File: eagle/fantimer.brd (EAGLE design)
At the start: 58 x 78 mm, 14 parts, among them IC3 PIC10F220, K1 PB2032-ND, Q1 2N7000-G, U1 IRM-01-5, X1 732-10957-ND

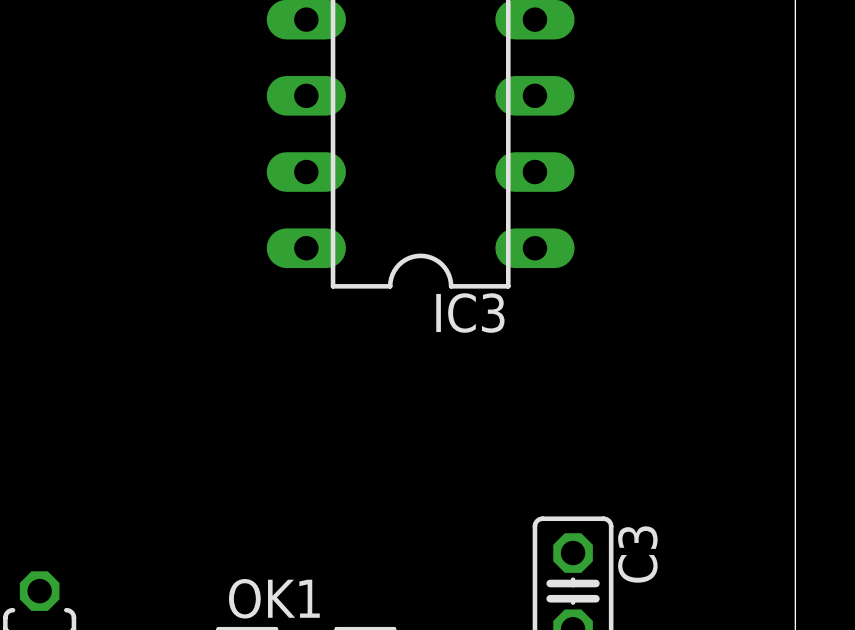
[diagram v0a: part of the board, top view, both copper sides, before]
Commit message: Renumber IC3 to IC1
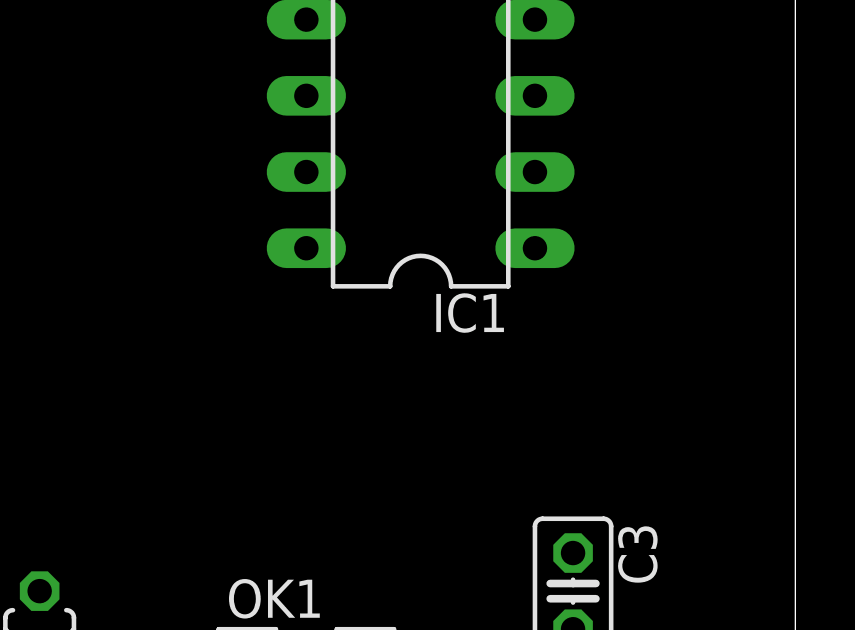
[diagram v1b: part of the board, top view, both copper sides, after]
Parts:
- renumbered IC3 to IC1
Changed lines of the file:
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@@
 <attribute name="SPICEPREFIX" value="X" x="45.72" y="48.26" size="1.778" layer="27" rot="R270" display="off"/>
 </element>
-<element name="IC3" library="ic-package" library_urn="urn:adsk.eagle:library:239" package="DIL08" package3d_urn="urn:adsk.eagle:package:14440/1" value="PIC10F220" x="43.18" y="22.86" rot="R90"/>
+<element name="IC1" library="ic-package" library_urn="urn:adsk.eagle:library:239" package="DIL08" package3d_urn="urn:adsk.eagle:package:14440/1" value="PIC10F220" x="43.18" y="22.86" rot="R90"/>
 <element name="C3" library="rcl" library_urn="urn:adsk.eagle:library:334" package="C025-025X050" package3d_urn="urn:adsk.eagle:package:23629/2" value="1uF" x="48.26" y="7.62" rot="R270">
 <attribute name="SPICEPREFIX" value="C" x="48.26" y="7.62" size="1.778" layer="27" rot="R270" display="off"/>
@@
 <signal name="FAN">
 <contactref element="Q1" pad="2"/>
-<contactref element="IC3" pad="5"/>
+<contactref element="IC1" pad="5"/>
 <wire x1="39.37" y1="26.67" x2="36.195" y2="35.56" width="0" layer="19" extent="1-1"/>
 </signal>
@@
 <signal name="!LIGHT">
 <contactref element="OK1" pad="4"/>
-<contactref element="IC3" pad="8"/>
+<contactref element="IC1" pad="8"/>
 <contactref element="C3" pad="2"/>
 <wire x1="43.18" y1="5.08" x2="39.37" y2="19.05" width="0" layer="19" extent="1-1"/>
@@
 <signal name="RTIMER">
 <contactref element="R3" pad="3"/>
-<contactref element="IC3" pad="4"/>
+<contactref element="IC1" pad="4"/>
 <wire x1="46.99" y1="26.67" x2="50.8" y2="48.26" width="0" layer="19" extent="1-1"/>
 </signal>
@@
 <contactref element="U1" pad="-V"/>
 <contactref element="OK1" pad="3"/>
-<contactref element="IC3" pad="7"/>
+<contactref element="IC1" pad="7"/>
 <contactref element="R3" pad="2"/>
 <wire x1="30.48" y1="45.74" x2="40.64" y2="45.72" width="0" layer="19" extent="1-1"/>
@@
 <contactref element="D1" pad="C"/>
 <contactref element="U1" pad="+V"/>
-<contactref element="IC3" pad="2"/>
+<contactref element="IC1" pad="2"/>
 <contactref element="R3" pad="1"/>
 <contactref element="C3" pad="1"/>

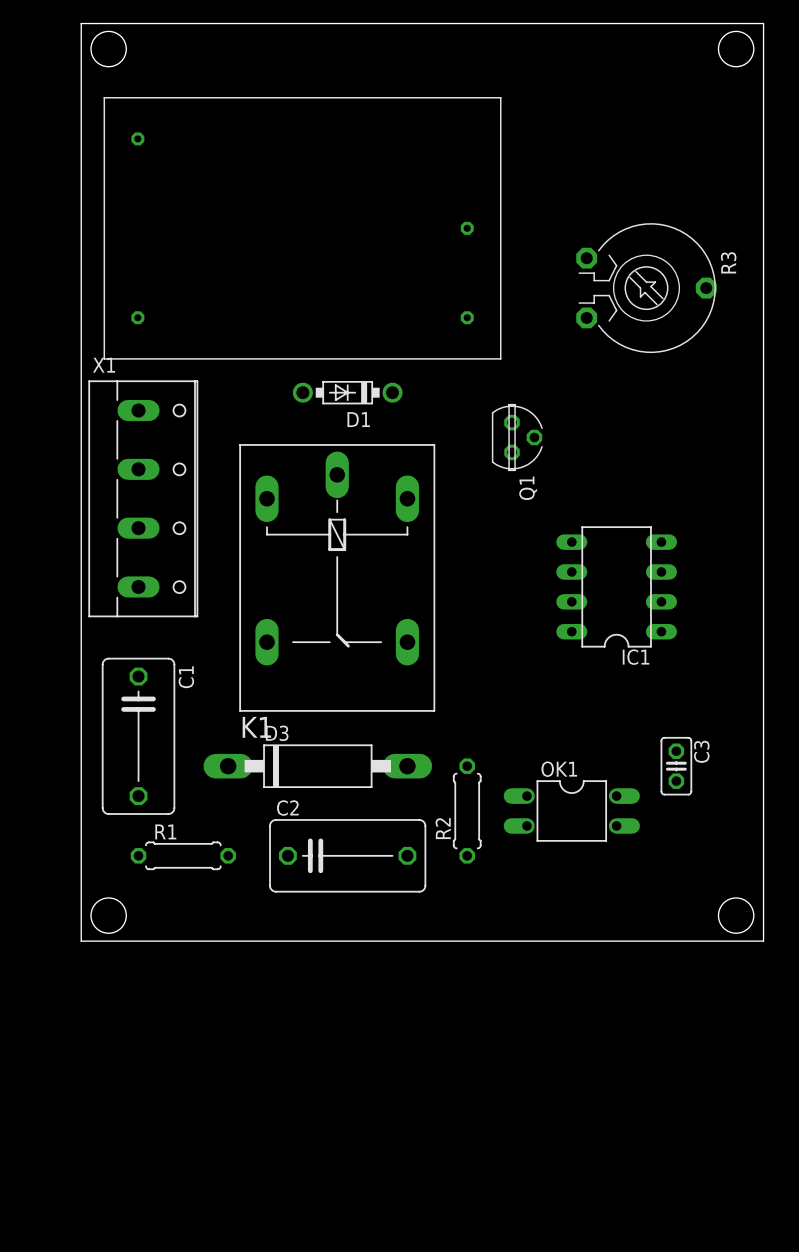
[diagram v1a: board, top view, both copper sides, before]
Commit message: Initial assembly. Add a better PIC Eagle lib. Remove PIC notes from sch.
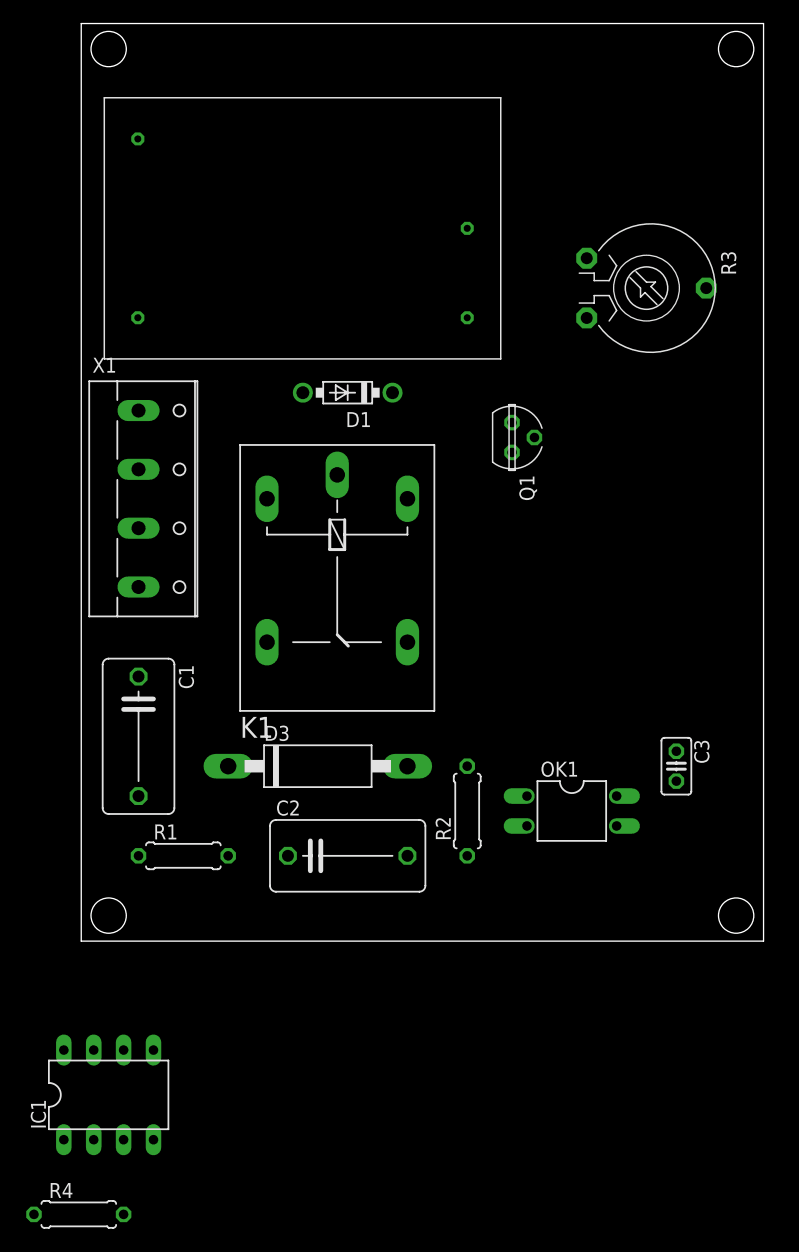
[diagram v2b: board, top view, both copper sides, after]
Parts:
- added R4: 10k, resistor:0207/7
- IC1: value PIC10F220 -> PIC10F200; device ic-package:DIL08 -> microchip-addl:DIL08
- moved IC1 61.1 mm to (0.00, -20.3), turned to 0 degrees
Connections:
- removed net RTIMER: IC1.4, R3.3
- new net ADJ: IC1.5, R3.3
- net !LIGHT: now also IC1.4; no longer IC1.8
- net FAN: now also IC1.3, R4.2; no longer IC1.5
- net GND: now also R4.1
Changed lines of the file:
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@@
 <attribute name="SPICEPREFIX" value="X" x="45.72" y="48.26" size="1.778" layer="27" rot="R270" display="off"/>
 </element>
-<element name="IC1" library="ic-package" library_urn="urn:adsk.eagle:library:239" package="DIL08" package3d_urn="urn:adsk.eagle:package:14440/1" value="PIC10F220" x="43.18" y="22.86" rot="R90"/>
 <element name="C3" library="rcl" library_urn="urn:adsk.eagle:library:334" package="C025-025X050" package3d_urn="urn:adsk.eagle:package:23629/2" value="1uF" x="48.26" y="7.62" rot="R270">
 <attribute name="SPICEPREFIX" value="C" x="48.26" y="7.62" size="1.778" layer="27" rot="R270" display="off"/>
 </element>
+<element name="IC1" library="microchip-addl" package="DIL08" package3d_urn="urn:adsk.eagle:package:14440/1" value="PIC10F200" x="0" y="-20.32"/>
+<element name="R4" library="resistor" library_urn="urn:adsk.eagle:library:348" package="0207/7" package3d_urn="urn:adsk.eagle:package:25942/1" value="10k" x="-2.54" y="-30.48"/>
 </elements>
 <signals>
@@
 <signal name="FAN">
 <contactref element="Q1" pad="2"/>
-<contactref element="IC1" pad="5"/>
-<wire x1="39.37" y1="26.67" x2="36.195" y2="35.56" width="0" layer="19" extent="1-1"/>
+<contactref element="IC1" pad="3"/>
+<contactref element="R4" pad="2"/>
+<wire x1="1.27" y1="-24.13" x2="36.195" y2="35.56" width="0" layer="19" extent="1-1"/>
+<wire x1="1.27" y1="-30.48" x2="1.27" y2="-24.13" width="0" layer="19" extent="1-1"/>
 </signal>
 <signal name="COILOUT">
@@
 <signal name="!LIGHT">
 <contactref element="OK1" pad="4"/>
-<contactref element="IC1" pad="8"/>
 <contactref element="C3" pad="2"/>
-<wire x1="43.18" y1="5.08" x2="39.37" y2="19.05" width="0" layer="19" extent="1-1"/>
-<wire x1="48.26" y1="6.35" x2="43.18" y2="5.08" width="0" layer="19" extent="1-1"/>
+<contactref element="IC1" pad="4"/>
+<wire x1="43.18" y1="5.08" x2="48.26" y2="6.35" width="0" layer="19" extent="1-1"/>
+<wire x1="3.81" y1="-24.13" x2="43.18" y2="5.08" width="0" layer="19" extent="1-1"/>
 </signal>
 <signal name="DETECT_IN">
@@
 <wire x1="2.54" y1="0" x2="2.54" y2="5.08" width="0" layer="19" extent="1-1"/>
 </signal>
-<signal name="RTIMER">
-<contactref element="R3" pad="3"/>
-<contactref element="IC1" pad="4"/>
-<wire x1="46.99" y1="26.67" x2="50.8" y2="48.26" width="0" layer="19" extent="1-1"/>
-</signal>
 <signal name="TIMER1">
 </signal>
@@
 <contactref element="U1" pad="-V"/>
 <contactref element="OK1" pad="3"/>
+<contactref element="R3" pad="2"/>
 <contactref element="IC1" pad="7"/>
-<contactref element="R3" pad="2"/>
+<contactref element="R4" pad="1"/>
 <wire x1="30.48" y1="45.74" x2="40.64" y2="45.72" width="0" layer="19" extent="1-1"/>
 <wire x1="34.29" y1="36.83" x2="30.48" y2="45.74" width="0" layer="19" extent="1-1"/>
-<wire x1="39.37" y1="21.59" x2="34.29" y2="36.83" width="0" layer="19" extent="1-1"/>
-<wire x1="43.18" y1="2.54" x2="39.37" y2="21.59" width="0" layer="19" extent="1-1"/>
+<wire x1="43.18" y1="2.54" x2="34.29" y2="36.83" width="0" layer="19" extent="1-1"/>
+<wire x1="-1.27" y1="-16.51" x2="43.18" y2="2.54" width="0" layer="19" extent="1-1"/>
+<wire x1="-6.35" y1="-30.48" x2="-1.27" y2="-16.51" width="0" layer="19" extent="1-1"/>
 </signal>
 <signal name="+5V">
@@
 <contactref element="D1" pad="C"/>
 <contactref element="U1" pad="+V"/>
+<contactref element="C3" pad="1"/>
+<contactref element="R3" pad="1"/>
 <contactref element="IC1" pad="2"/>
-<contactref element="R3" pad="1"/>
-<contactref element="C3" pad="1"/>
 <wire x1="30.48" y1="53.34" x2="40.64" y2="50.8" width="0" layer="19" extent="1-1"/>
 <wire x1="24.13" y1="39.37" x2="30.48" y2="53.34" width="0" layer="19" extent="1-1"/>
 <wire x1="25.4" y1="30.353" x2="24.13" y2="39.37" width="0" layer="19" extent="1-1"/>
-<wire x1="46.99" y1="21.59" x2="25.4" y2="30.353" width="0" layer="19" extent="1-1"/>
-<wire x1="48.26" y1="8.89" x2="46.99" y2="21.59" width="0" layer="19" extent="1-1"/>
+<wire x1="48.26" y1="8.89" x2="25.4" y2="30.353" width="0" layer="19" extent="1-1"/>
+<wire x1="-1.27" y1="-24.13" x2="48.26" y2="8.89" width="0" layer="19" extent="1-1"/>
+</signal>
+<signal name="ADJ">
+<contactref element="R3" pad="3"/>
+<contactref element="IC1" pad="5"/>
+<wire x1="3.81" y1="-16.51" x2="50.8" y2="48.26" width="0" layer="19" extent="1-1"/>
 </signal>
 </signals>

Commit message: Add filter cap for MCU
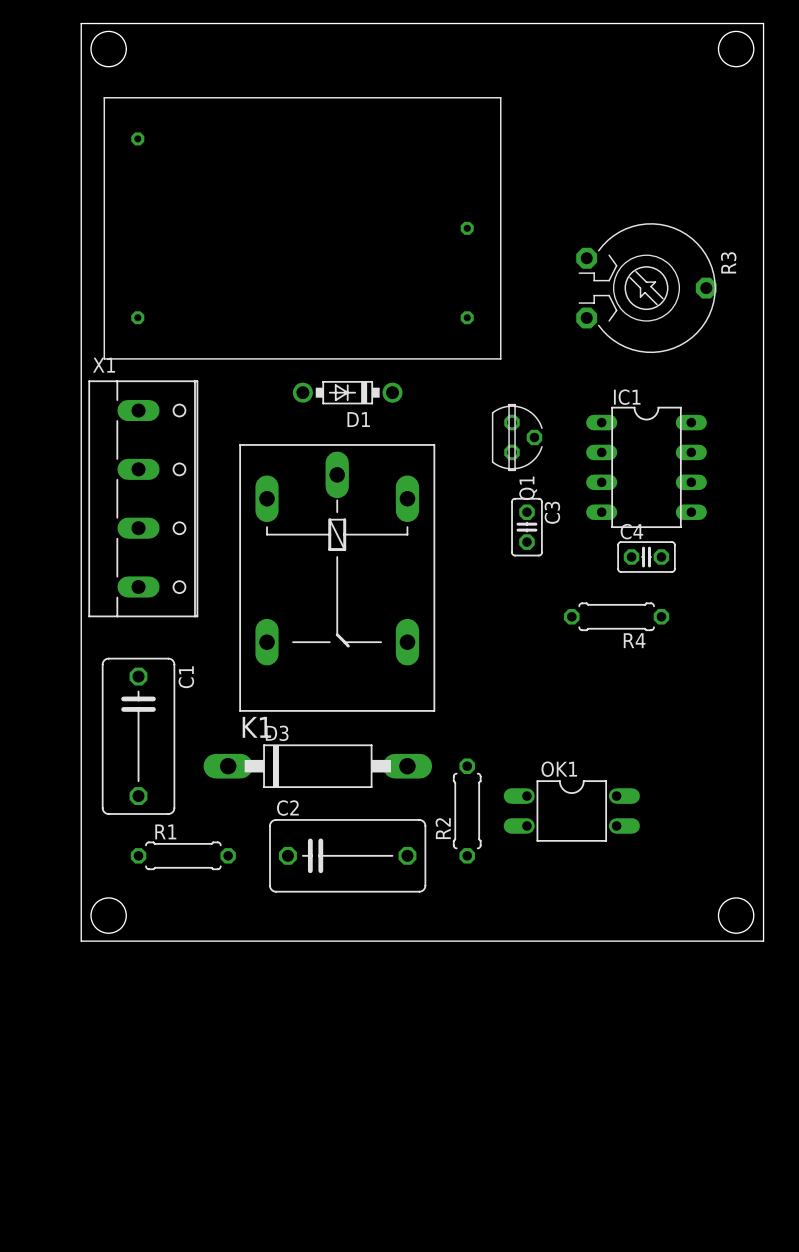
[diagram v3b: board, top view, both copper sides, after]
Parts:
- added C4: 1uF, rcl:C025-025X050
- moved IC1 70.3 mm to (45.7, 33.0), turned to 270 degrees
- moved R4 68.3 mm to (43.2, 20.3), turned to 180 degrees
- moved C3 24.0 mm to (35.6, 27.9)
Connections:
- net +5V: now also C4.1
- net GND: now also C4.2
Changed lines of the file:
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@@
 <attribute name="SPICEPREFIX" value="X" x="45.72" y="48.26" size="1.778" layer="27" rot="R270" display="off"/>
 </element>
-<element name="C3" library="rcl" library_urn="urn:adsk.eagle:library:334" package="C025-025X050" package3d_urn="urn:adsk.eagle:package:23629/2" value="1uF" x="48.26" y="7.62" rot="R270">
-<attribute name="SPICEPREFIX" value="C" x="48.26" y="7.62" size="1.778" layer="27" rot="R270" display="off"/>
+<element name="C3" library="rcl" library_urn="urn:adsk.eagle:library:334" package="C025-025X050" package3d_urn="urn:adsk.eagle:package:23629/2" value="1uF" x="35.56" y="27.94" rot="R270">
+<attribute name="SPICEPREFIX" value="C" x="35.56" y="27.94" size="1.778" layer="27" rot="R270" display="off"/>
 </element>
-<element name="IC1" library="microchip-addl" package="DIL08" package3d_urn="urn:adsk.eagle:package:14440/1" value="PIC10F200" x="0" y="-20.32"/>
-<element name="R4" library="resistor" library_urn="urn:adsk.eagle:library:348" package="0207/7" package3d_urn="urn:adsk.eagle:package:25942/1" value="10k" x="-2.54" y="-30.48"/>
+<element name="IC1" library="microchip-addl" package="DIL08" package3d_urn="urn:adsk.eagle:package:14440/1" value="PIC10F200" x="45.72" y="33.02" rot="R270"/>
+<element name="R4" library="resistor" library_urn="urn:adsk.eagle:library:348" package="0207/7" package3d_urn="urn:adsk.eagle:package:25942/1" value="10k" x="43.18" y="20.32" rot="R180"/>
+<element name="C4" library="rcl" library_urn="urn:adsk.eagle:library:334" package="C025-025X050" package3d_urn="urn:adsk.eagle:package:23629/2" value="1uF" x="45.72" y="25.4">
+<attribute name="SPICEPREFIX" value="C" x="45.72" y="25.4" size="1.778" layer="27" display="off"/>
+</element>
 </elements>
 <signals>
@@
 <contactref element="IC1" pad="3"/>
 <contactref element="R4" pad="2"/>
-<wire x1="1.27" y1="-24.13" x2="36.195" y2="35.56" width="0" layer="19" extent="1-1"/>
-<wire x1="1.27" y1="-30.48" x2="1.27" y2="-24.13" width="0" layer="19" extent="1-1"/>
+<wire x1="41.91" y1="31.75" x2="36.195" y2="35.56" width="0" layer="19" extent="1-1"/>
+<wire x1="39.37" y1="20.32" x2="41.91" y2="31.75" width="0" layer="19" extent="1-1"/>
 </signal>
 <signal name="COILOUT">
@@
 <contactref element="C3" pad="2"/>
 <contactref element="IC1" pad="4"/>
-<wire x1="43.18" y1="5.08" x2="48.26" y2="6.35" width="0" layer="19" extent="1-1"/>
-<wire x1="3.81" y1="-24.13" x2="43.18" y2="5.08" width="0" layer="19" extent="1-1"/>
+<wire x1="35.56" y1="26.67" x2="41.91" y2="29.21" width="0" layer="19" extent="1-1"/>
+<wire x1="43.18" y1="5.08" x2="35.56" y2="26.67" width="0" layer="19" extent="1-1"/>
 </signal>
 <signal name="DETECT_IN">
@@
 <contactref element="IC1" pad="7"/>
 <contactref element="R4" pad="1"/>
+<contactref element="C4" pad="2"/>
 <wire x1="30.48" y1="45.74" x2="40.64" y2="45.72" width="0" layer="19" extent="1-1"/>
 <wire x1="34.29" y1="36.83" x2="30.48" y2="45.74" width="0" layer="19" extent="1-1"/>
-<wire x1="43.18" y1="2.54" x2="34.29" y2="36.83" width="0" layer="19" extent="1-1"/>
-<wire x1="-1.27" y1="-16.51" x2="43.18" y2="2.54" width="0" layer="19" extent="1-1"/>
-<wire x1="-6.35" y1="-30.48" x2="-1.27" y2="-16.51" width="0" layer="19" extent="1-1"/>
+<wire x1="49.53" y1="34.29" x2="40.64" y2="45.72" width="0" layer="19" extent="1-1"/>
+<wire x1="46.99" y1="25.4" x2="49.53" y2="34.29" width="0" layer="19" extent="1-1"/>
+<wire x1="46.99" y1="20.32" x2="46.99" y2="25.4" width="0" layer="19" extent="1-1"/>
+<wire x1="43.18" y1="2.54" x2="46.99" y2="20.32" width="0" layer="19" extent="1-1"/>
 </signal>
 <signal name="+5V">
@@
 <contactref element="R3" pad="1"/>
 <contactref element="IC1" pad="2"/>
+<contactref element="C4" pad="1"/>
 <wire x1="30.48" y1="53.34" x2="40.64" y2="50.8" width="0" layer="19" extent="1-1"/>
 <wire x1="24.13" y1="39.37" x2="30.48" y2="53.34" width="0" layer="19" extent="1-1"/>
 <wire x1="25.4" y1="30.353" x2="24.13" y2="39.37" width="0" layer="19" extent="1-1"/>
-<wire x1="48.26" y1="8.89" x2="25.4" y2="30.353" width="0" layer="19" extent="1-1"/>
-<wire x1="-1.27" y1="-24.13" x2="48.26" y2="8.89" width="0" layer="19" extent="1-1"/>
+<wire x1="35.56" y1="29.21" x2="25.4" y2="30.353" width="0" layer="19" extent="1-1"/>
+<wire x1="41.91" y1="34.29" x2="35.56" y2="29.21" width="0" layer="19" extent="1-1"/>
+<wire x1="44.45" y1="25.4" x2="41.91" y2="34.29" width="0" layer="19" extent="1-1"/>
 </signal>
 <signal name="ADJ">
 <contactref element="R3" pad="3"/>
 <contactref element="IC1" pad="5"/>
-<wire x1="3.81" y1="-16.51" x2="50.8" y2="48.26" width="0" layer="19" extent="1-1"/>
+<wire x1="49.53" y1="29.21" x2="50.8" y2="48.26" width="0" layer="19" extent="1-1"/>
 </signal>
 </signals>

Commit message: Some wire rearranging
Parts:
- moved R4 23.4 mm to (38.1, 43.2), turned to 270 degrees
- moved C4 12.7 mm to (45.7, 38.1)
- moved C2 8.03 mm to (17.8, 7.62)
- moved D3 8.03 mm to (20.3, 0.00)
- moved IC1 7.62 mm to (45.7, 25.4)
- moved R3 5.68 mm to (48.3, 53.3)
- moved C3 5.08 mm to (35.6, 22.9)
- moved R1 4.02 mm to (7.62, 3.81), turned to 90 degrees
- moved R2 4.02 mm to (29.2, 7.62), turned to 0 degrees
- moved OK1 3.59 mm to (41.9, 6.35)
- moved Q1 2.54 mm to (34.3, 33.0)
